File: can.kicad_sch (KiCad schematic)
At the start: 11 parts, among them U4 SN65HVD230

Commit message: v2 time
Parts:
- JP3: renamed from JP?; footprint (none) -> Jumper:SolderJumper-2_P1.3mm_Open_RoundedPad1.0x1.5mm
- gave numbers to parts that had none: 9
- renumbered U4 to U20
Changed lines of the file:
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@@
   (symbol (lib_id "power:GND") (at 134.62 99.06 0) (unit 1)
     (in_bom yes) (on_board yes) (fields_autoplaced)
-    (property "Reference" "#PWR?" (id 0) (at 134.62 105.41 0)
+    (property "Reference" "#PWR0123" (id 0) (at 134.62 105.41 0)
       (effects (font (size 1.27 1.27)) hide)
     )
@@
   (symbol (lib_id "power:+3.3V") (at 124.46 68.58 0) (unit 1)
     (in_bom yes) (on_board yes) (fields_autoplaced)
-    (property "Reference" "#PWR?" (id 0) (at 124.46 72.39 0)
+    (property "Reference" "#PWR0121" (id 0) (at 124.46 72.39 0)
       (effects (font (size 1.27 1.27)) hide)
     )
@@
   (symbol (lib_id "Interface_CAN_LIN:SN65HVD230") (at 134.62 87.63 0) (unit 1)
     (in_bom yes) (on_board yes) (fields_autoplaced)
-    (property "Reference" "U?" (id 0) (at 142.24 75.1586 0))
+    (property "Reference" "U20" (id 0) (at 142.24 75.1586 0))
     (property "Value" "SN65HVD230" (id 1) (at 142.24 77.47 0))
     (property "Footprint" "Package_SO:SOIC-8_3.9x4.9mm_P1.27mm" (id 2) (at 134.62 100.33 0)
@@
   (symbol (lib_id "Device:C_Small") (at 127 71.12 0) (unit 1)
     (in_bom yes) (on_board yes) (fields_autoplaced)
-    (property "Reference" "C?" (id 0) (at 129.54 69.8562 0)
+    (property "Reference" "C51" (id 0) (at 129.54 69.8562 0)
       (effects (font (size 1.27 1.27)) (justify left))
     )
@@
   (symbol (lib_id "Device:C_Small") (at 175.26 82.55 180) (unit 1)
     (in_bom yes) (on_board yes)
-    (property "Reference" "C?" (id 0) (at 173.99 74.93 0)
+    (property "Reference" "C53" (id 0) (at 173.99 74.93 0)
       (effects (font (size 1.27 1.27)) (justify right))
     )
@@
   (symbol (lib_id "Diode:SM712_SOT23") (at 186.69 88.9 270) (unit 1)
     (in_bom yes) (on_board yes) (fields_autoplaced)
-    (property "Reference" "D?" (id 0) (at 190.5 87.63 90)
+    (property "Reference" "D11" (id 0) (at 190.5 87.63 90)
       (effects (font (size 1.27 1.27)) (justify left))
     )
@@
   (symbol (lib_id "power:GND") (at 175.26 88.9 0) (unit 1)
     (in_bom yes) (on_board yes) (fields_autoplaced)
-    (property "Reference" "#PWR?" (id 0) (at 175.26 95.25 0)
+    (property "Reference" "#PWR0124" (id 0) (at 175.26 95.25 0)
       (effects (font (size 1.27 1.27)) hide)
     )
@@
   (symbol (lib_id "power:GND") (at 175.26 102.87 0) (unit 1)
     (in_bom yes) (on_board yes) (fields_autoplaced)
-    (property "Reference" "#PWR?" (id 0) (at 175.26 109.22 0)
+    (property "Reference" "#PWR0125" (id 0) (at 175.26 109.22 0)
       (effects (font (size 1.27 1.27)) hide)
     )
@@
   (symbol (lib_id "Device:C_Small") (at 121.92 71.12 0) (unit 1)
     (in_bom yes) (on_board yes) (fields_autoplaced)
-    (property "Reference" "C?" (id 0) (at 114.3 69.85 0)
+    (property "Reference" "C50" (id 0) (at 114.3 69.85 0)
       (effects (font (size 1.27 1.27)) (justify left))
     )
@@
   (symbol (lib_id "Device:R_Small") (at 124.46 95.25 0) (unit 1)
     (in_bom yes) (on_board yes)
-    (property "Reference" "R?" (id 0) (at 118.11 93.98 0)
+    (property "Reference" "R31" (id 0) (at 118.11 93.98 0)
       (effects (font (size 1.27 1.27)) (justify left))
     )
@@
   (symbol (lib_id "Device:R") (at 167.64 93.98 0) (unit 1)
     (in_bom yes) (on_board yes) (fields_autoplaced)
-    (property "Reference" "R?" (id 0) (at 162.56 92.71 0)
+    (property "Reference" "R33" (id 0) (at 162.56 92.71 0)
       (effects (font (size 1.27 1.27)) (justify left))
     )
@@
   (symbol (lib_id "Device:R") (at 167.64 83.82 0) (unit 1)
     (in_bom yes) (on_board yes) (fields_autoplaced)
-    (property "Reference" "R?" (id 0) (at 162.56 82.55 0)
+    (property "Reference" "R32" (id 0) (at 162.56 82.55 0)
       (effects (font (size 1.27 1.27)) (justify left))
     )
@@
   (symbol (lib_id "Device:C") (at 171.45 88.9 90) (unit 1)
     (in_bom yes) (on_board yes) (fields_autoplaced)
-    (property "Reference" "C?" (id 0) (at 171.45 82.55 90))
+    (property "Reference" "C52" (id 0) (at 171.45 82.55 90))
     (property "Value" "0.1uF" (id 1) (at 171.45 85.09 90))
     (property "Footprint" "Capacitor_SMD:C_0402_1005Metric" (id 2) (at 175.26 87.9348 0)
@@
   (symbol (lib_id "power:GND") (at 124.46 73.66 0) (unit 1)
     (in_bom yes) (on_board yes) (fields_autoplaced)
-    (property "Reference" "#PWR?" (id 0) (at 124.46 80.01 0)
+    (property "Reference" "#PWR0122" (id 0) (at 124.46 80.01 0)
       (effects (font (size 1.27 1.27)) hide)
     )
@@
   (symbol (lib_id "Jumper:SolderJumper_2_Open") (at 157.48 88.9 0) (unit 1)
     (in_bom yes) (on_board yes) (fields_autoplaced)
-    (property "Reference" "JP?" (id 0) (at 157.48 82.55 0))
+    (property "Reference" "JP3" (id 0) (at 157.48 82.55 0))
     (property "Value" "TermJP" (id 1) (at 157.48 85.09 0))
-    (property "Footprint" "" (id 2) (at 157.48 88.9 0)
+    (property "Footprint" "Jumper:SolderJumper-2_P1.3mm_Open_RoundedPad1.0x1.5mm" (id 2) (at 157.48 88.9 0)
       (effects (font (size 1.27 1.27)) hide)
     )
@@
   (symbol (lib_id "Device:C_Small") (at 175.26 100.33 180) (unit 1)
     (in_bom yes) (on_board yes) (fields_autoplaced)
-    (property "Reference" "C?" (id 0) (at 177.8 99.0535 0)
+    (property "Reference" "C54" (id 0) (at 177.8 99.0535 0)
       (effects (font (size 1.27 1.27)) (justify right))
     )

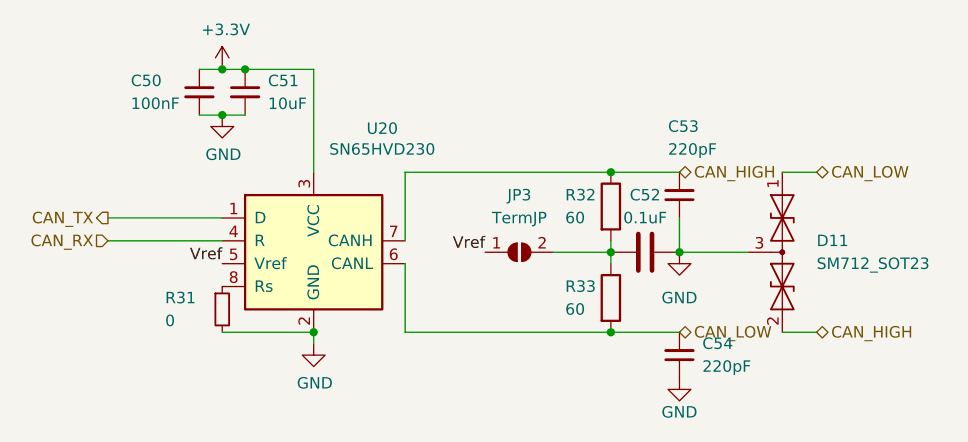
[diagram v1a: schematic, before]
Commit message: changed bb and power side
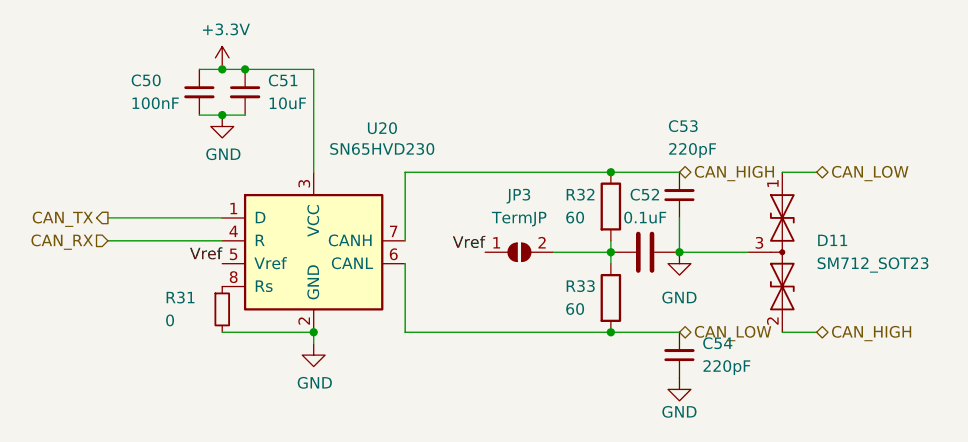
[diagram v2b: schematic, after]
